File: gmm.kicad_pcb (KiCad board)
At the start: 6 copper layers, 70 x 50 mm, 260 parts, among them P1 10144518-061802LF, P2 10144518-061802LF, P3 10144518-061802LF, P4 10144518-061802LF, P5 10144518-061802LF, U1 CCGM1A1, U10 PCA9539AHF, U11 TPS3840DL28DBV, U12 TPS7A91, U13 ADP151ACP, U2 5P49V6965, U3 TPS65266, U4 STG3692, U5 STG3692, U6 74LVC1G08, U7 74LVC1G07, U8 STG3692, U9 IS25LQ032B-JNLE, Y1 NX3225SA

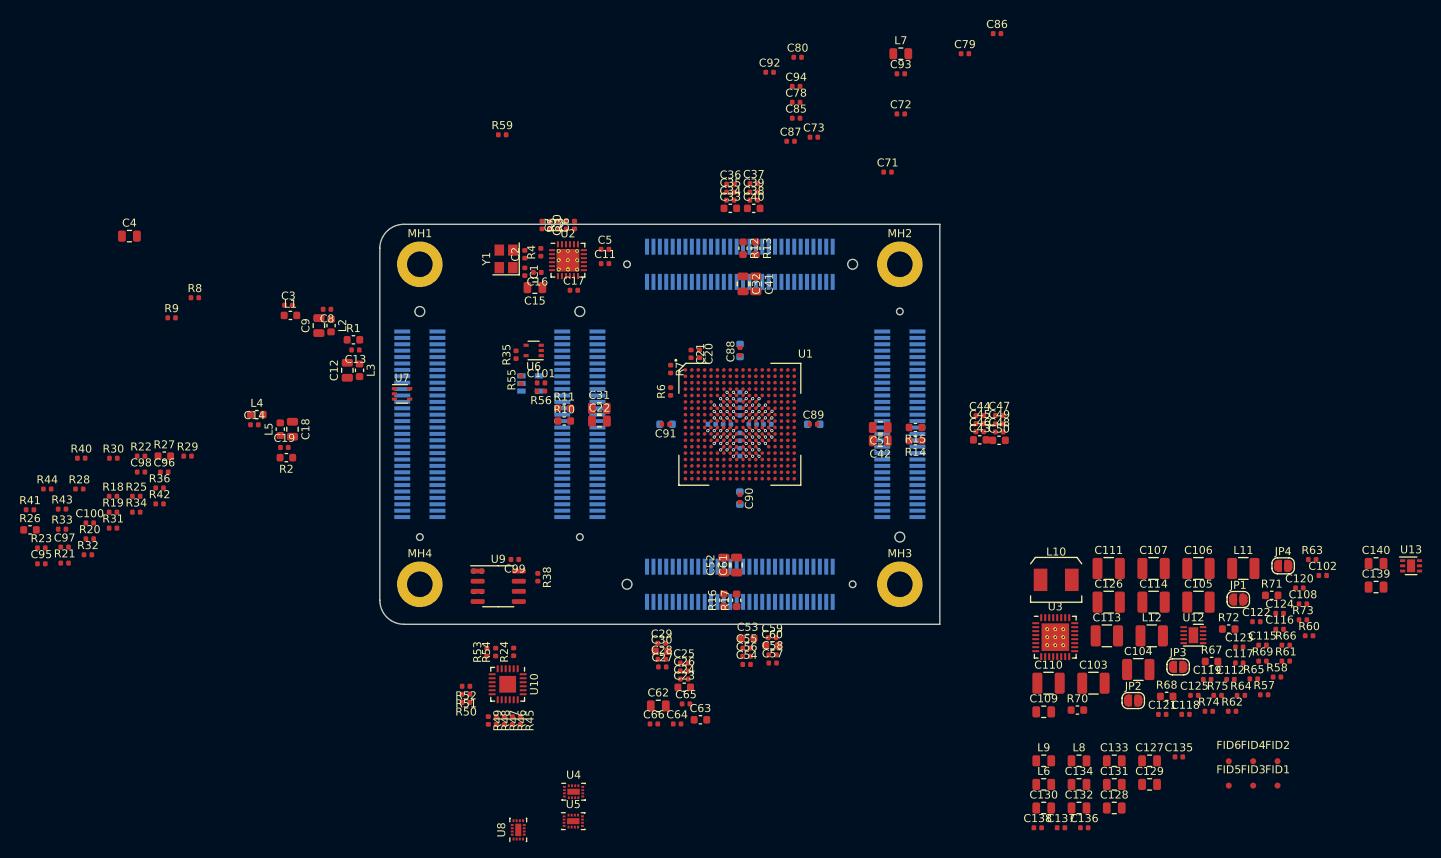
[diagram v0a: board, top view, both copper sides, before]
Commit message: Schematic freeze, preliminary placement is done.
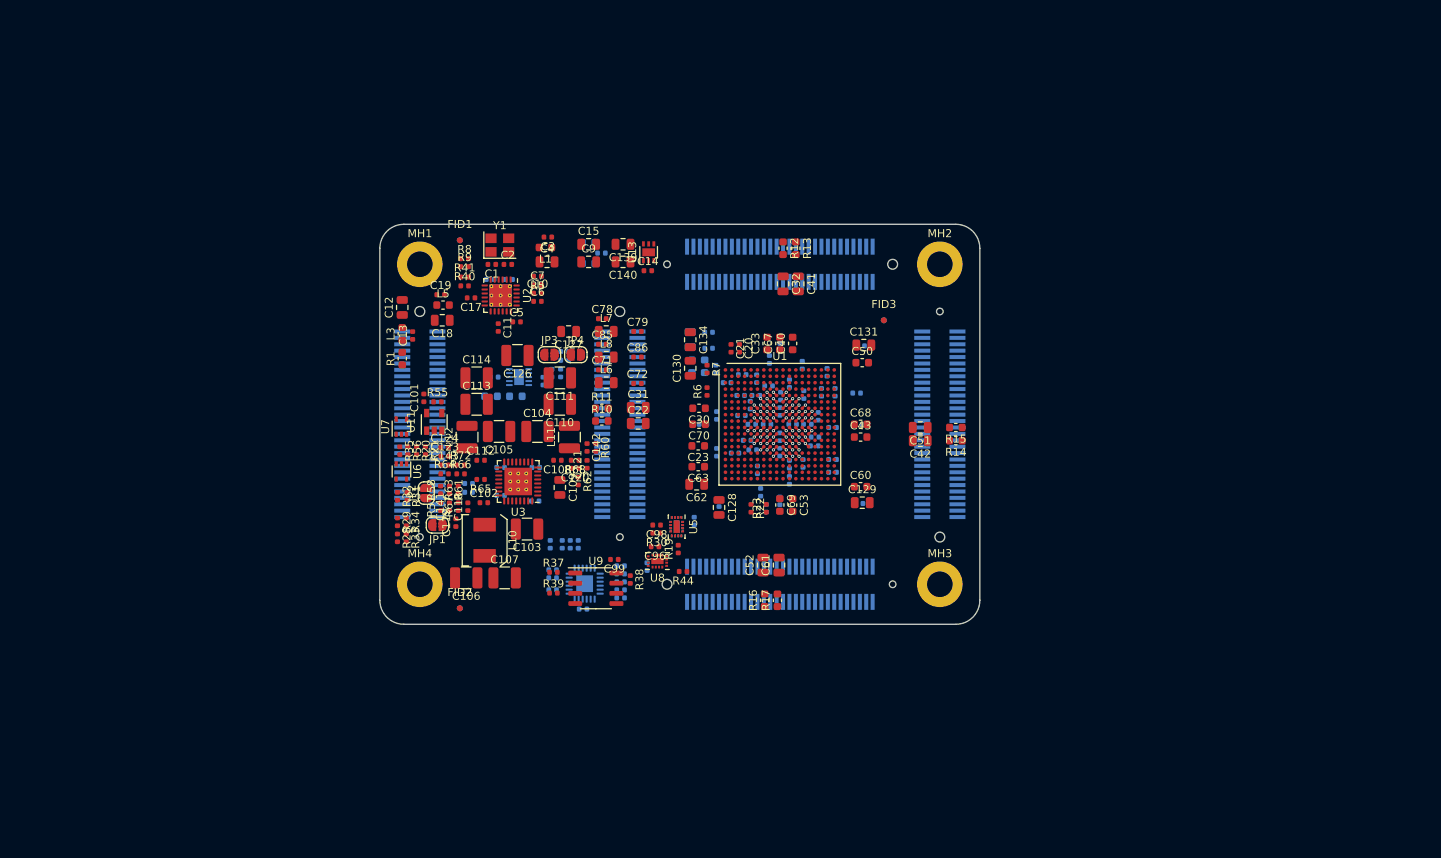
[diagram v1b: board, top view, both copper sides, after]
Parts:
- removed C132, C133: 2.2uF, Capacitor_SMD:C_0805_2012Metric
- removed R2: DNI, Resistor_SMD:R_0603_1608Metric
- added C141: DNI, Capacitor_SMD:C_0402_1005Metric, F.Cu at (98.7, 115.3)
- added C142: DNI, Capacitor_SMD:C_0402_1005Metric, F.Cu at (115.9, 107.9)
- added C143: DNI, Capacitor_SMD:C_0402_1005Metric, F.Cu at (98.1, 110.1)
- C100, C115, C116, C117, C122, C125, C135, C136, C137, C138, C16, C24, C25, C26, C27, C28, C29, C34, C35, C36, C37, C38, C39, C44, C45, C46, C47, C48, C49, C54, C55, C56, C57, C58, C59, C64, C65, C66, C73, C8, C80, C87, C88, C89, C90, C91, C92, C93, C94, C95, C97, FID4, FID5, FID6, L2, L4, L9, R18, R24, R25, R26, R27, R3, R36, R4, R42, R43, R45, R46, R47, R48, R49, R50, R51, R52, R53, R54, R59, R69, R70, R71, R73, R74, R75, U10, U12, U4: moved to B.Cu
- C67, C68, C69, C70, R37, R39, U11: moved to F.Cu
- R67, R68, R72: footprint Resistor_SMD:R_0603_1608Metric -> Resistor_SMD:R_0402_1005Metric
- moved FID1 122.9 mm to (100.0, 82.0)
- moved FID4 118.6 mm to (100.0, 82.0)
- moved R58 107.1 mm to (97.6, 113.2), turned to 90 degrees
- moved R63 107.1 mm to (99.8, 113.2), turned to 90 degrees
- moved R61 106.7 mm to (98.7, 113.2), turned to 270 degrees
- moved C124 106.4 mm to (98.1, 107.9)
- moved R57 105.6 mm to (97.6, 115.3), turned to 90 degrees
- moved R66 105.3 mm to (100.1, 111.2)
- moved C102 105.3 mm to (103.0, 114.8)
- moved FID2 104.0 mm to (100.0, 128.0)
- moved C139 103.4 mm to (120.4, 82.5), turned to 180 degrees
- moved R64 103.3 mm to (98.1, 111.2)
- moved U13 103.1 mm to (123.6, 83.5), turned to 90 degrees
- moved C123 102.1 mm to (98.1, 109.0)
- moved C140 101.4 mm to (120.4, 84.7), turned to 180 degrees
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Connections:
- net Net-(C102-Pad1) renamed /Power Converter/LX1
- net Net-(C102-Pad2) renamed /Power Converter/BST1
- net Net-(C108-Pad1) renamed /Power Converter/LX2
- net Net-(C108-Pad2) renamed /Power Converter/BST2
- net Net-(C112-Pad1) renamed /Power Converter/LX3
- net Net-(C112-Pad2) renamed /Power Converter/BST3
- net Net-(C115-Pad1) renamed /Power Converter/SS1
- net Net-(C116-Pad1) renamed /Power Converter/SS2
- net Net-(C117-Pad1) renamed /Power Converter/SS3
- net Net-(R60-Pad2) renamed /Power Converter/FB2
- net Net-(R61-Pad2) renamed /Power Converter/FB1
- net Net-(R64-Pad2) renamed /Power Converter/FB3
- C13 pad 1: VCLKO3 -> VCLK
- C19 pad 1: VCLKO4 -> VCLK
- C20 pad 1: (no net) -> TX_P
- C21 pad 1: (no net) -> TX_N
- L3 pad 1: VCLKO3 -> VCLK
- L5 pad 1: VCLKO4 -> VCLK
- P5 pad 1: (no net) -> GND
- P5 pad 10: (no net) -> SPI_CS_N
- P5 pad 11: (no net) -> SPI_D3
- P5 pad 12: (no net) -> SPI_D1
- P5 pad 13: (no net) -> GND
- P5 pad 14: (no net) -> SPI_FWD
- P5 pad 15: (no net) -> JTAG_TCK
- P5 pad 16: (no net) -> GND
- P5 pad 17: (no net) -> JTAG_TMS
- P5 pad 18: (no net) -> CFG_FAILED_N
- P5 pad 19: (no net) -> JTAG_TDI
- P5 pad 2: (no net) -> GND
- P5 pad 20: (no net) -> CFG_DONE
- P5 pad 21: (no net) -> JTAG_TDO
- P5 pad 22: (no net) -> GND
- P5 pad 23: (no net) -> GND
- P5 pad 24: (no net) -> +2V5
- P5 pad 25: (no net) -> V_IN
- P5 pad 26: (no net) -> V_IN
- P5 pad 27: (no net) -> V_IN
- P5 pad 28: (no net) -> V_IN
- P5 pad 29: (no net) -> V_IN
- P5 pad 3: (no net) -> SPI_CLK
- P5 pad 30: (no net) -> V_IN
- P5 pad 31: (no net) -> V_IN
- P5 pad 32: (no net) -> V_IN
- P5 pad 33: (no net) -> V_IN
- P5 pad 34: (no net) -> V_IN
- P5 pad 35: (no net) -> GND
- P5 pad 36: (no net) -> GND
- P5 pad 37: (no net) -> MR_N
- P5 pad 38: (no net) -> OFF_N
- P5 pad 39: (no net) -> RST_N
- P5 pad 4: (no net) -> SDA
- P5 pad 40: (no net) -> +2V5
- P5 pad 41: (no net) -> GND
- P5 pad 42: (no net) -> GND
- P5 pad 43: (no net) -> TX_N
- P5 pad 44: (no net) -> RX_N
- P5 pad 45: (no net) -> TX_P
- P5 pad 46: (no net) -> RX_P
- P5 pad 47: (no net) -> GND
- P5 pad 48: (no net) -> GND
- P5 pad 49: (no net) -> CLK2_P
- P5 pad 5: (no net) -> GND
- P5 pad 50: (no net) -> CLK3_P
- P5 pad 51: (no net) -> CLK2_N
- P5 pad 52: (no net) -> CLK3_N
- P5 pad 53: (no net) -> GND
- P5 pad 54: (no net) -> VCLK
- P5 pad 55: (no net) -> CLKI_P
- P5 pad 56: (no net) -> CLK4_N
- P5 pad 57: (no net) -> CLKI_N
- P5 pad 58: (no net) -> CLK4_P
- P5 pad 59: (no net) -> GND
- P5 pad 6: (no net) -> SCL
- P5 pad 60: (no net) -> GND
- P5 pad 7: (no net) -> SPI_D0
- P5 pad 8: (no net) -> GND
- P5 pad 9: (no net) -> SPI_D2
- R1 pad 2: VCLKO3 -> VCLK
- R22 pad 2: (no net) -> JTAG_TDO
- R25 pad 1: (no net) -> SPI_FWD
- R29 pad 1: (no net) -> SPI_D0
- R31 pad 1: (no net) -> SPI_D1
- R32 pad 1: (no net) -> SPI_CS_N
- R34 pad 1: (no net) -> SPI_CLK
- R36 pad 1: (no net) -> SPI_D2
- R42 pad 1: (no net) -> SPI_D3
- U1 pad B1: (no net) -> RX_P
- U1 pad C1: (no net) -> RX_N
- U2 pad 11: (no net) -> CLK4_P
- U2 pad 12: (no net) -> CLK4_N
- U2 pad 13: (no net) -> CLK3_N
- U2 pad 14: (no net) -> CLK3_P
- U2 pad 16: (no net) -> CLK2_N
- U2 pad 17: (no net) -> CLK2_P
- U7 pad 4: (no net) -> RST_N
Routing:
- net VIO_E1: track 1.13 -> 1.70 mm
- net VIO_S2: track 0.57 -> 1.13 mm
- net VIO_S1: track 1.70 -> 2.26 mm
- net GND: vias 37 -> 36
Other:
- board size 70 x 50 mm -> 75 x 50 mm
